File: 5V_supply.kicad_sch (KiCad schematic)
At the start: 25 parts

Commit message: little change
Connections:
- net VCC is gone; now on net 24V_supply: Q?.5 (D), Q?.6 (D), Q?.7 (D), Q?.8 (D)
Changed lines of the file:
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@@
   (junction (at 133.35 101.6) (diameter 0) (color 0 0 0 0)
   )
-  (junction (at 157.48 69.85) (diameter 0) (color 0 0 0 0)
-  )
   (junction (at 181.61 97.79) (diameter 0) (color 0 0 0 0)
   )
@@
     (stroke (width 0) (type default) (color 0 0 0 0))
   )
+  (wire (pts (xy 157.48 53.34) (xy 157.48 72.39))
+    (stroke (width 0) (type default) (color 0 0 0 0))
+  )
   (wire (pts (xy 102.87 95.25) (xy 102.87 97.79))
     (stroke (width 0) (type default) (color 0 0 0 0))
@@
     (stroke (width 0) (type default) (color 0 0 0 0))
   )
+  (wire (pts (xy 73.66 62.23) (xy 73.66 53.34))
+    (stroke (width 0) (type default) (color 0 0 0 0))
+  )
   (wire (pts (xy 118.11 69.85) (xy 118.11 74.93))
     (stroke (width 0) (type default) (color 0 0 0 0))
@@
     (stroke (width 0) (type default) (color 0 0 0 0))
   )
-  (wire (pts (xy 157.48 67.31) (xy 157.48 69.85))
-    (stroke (width 0) (type default) (color 0 0 0 0))
-  )
   (wire (pts (xy 110.49 62.23) (xy 110.49 69.85))
     (stroke (width 0) (type default) (color 0 0 0 0))
@@
     (stroke (width 0) (type default) (color 0 0 0 0))
   )
-  (wire (pts (xy 157.48 69.85) (xy 157.48 72.39))
-    (stroke (width 0) (type default) (color 0 0 0 0))
-  )
   (wire (pts (xy 130.81 92.71) (xy 149.86 92.71))
     (stroke (width 0) (type default) (color 0 0 0 0))
@@
   )
   (wire (pts (xy 186.69 82.55) (xy 194.31 82.55))
+    (stroke (width 0) (type default) (color 0 0 0 0))
+  )
+  (wire (pts (xy 73.66 53.34) (xy 157.48 53.34))
     (stroke (width 0) (type default) (color 0 0 0 0))
   )
@@
     (pin "2")
   )
-  (symbol (lib_id "power:VCC") (at 157.48 69.85 0) (unit 1)
-    (in_bom yes) (on_board yes) (fields_autoplaced)
-    (property "Reference" "#PWR?" (id 0) (at 157.48 73.66 0)
-      (effects (font (size 1.27 1.27)) hide)
-    )
-    (property "Value" "VCC" (id 1) (at 157.48 66.2455 0))
-    (property "Footprint" "" (id 2) (at 157.48 69.85 0)
-      (effects (font (size 1.27 1.27)) hide)
-    )
-    (property "Datasheet" "" (id 3) (at 157.48 69.85 0)
-      (effects (font (size 1.27 1.27)) hide)
-    )
-    (pin "1")
-  )
   (symbol (lib_id "Device:R") (at 139.7 101.6 90) (unit 1)

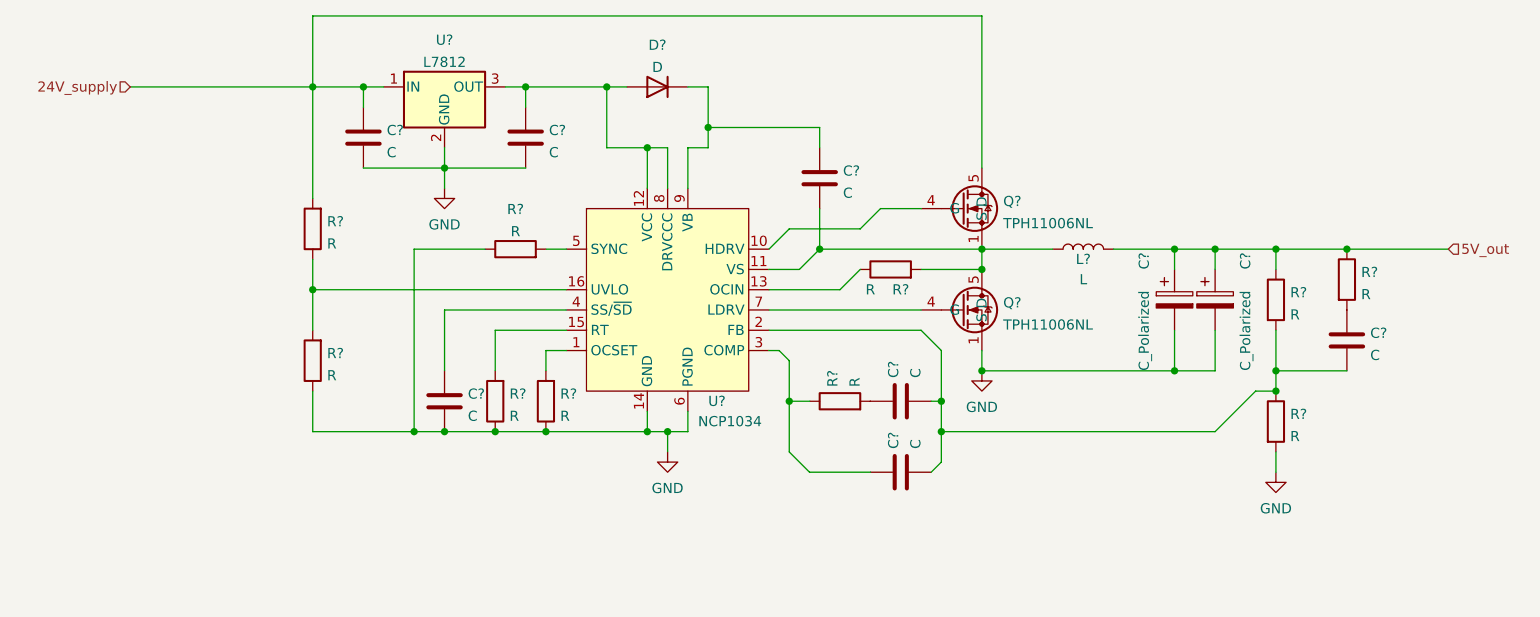
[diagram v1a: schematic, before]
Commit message: DC-DC pram setted
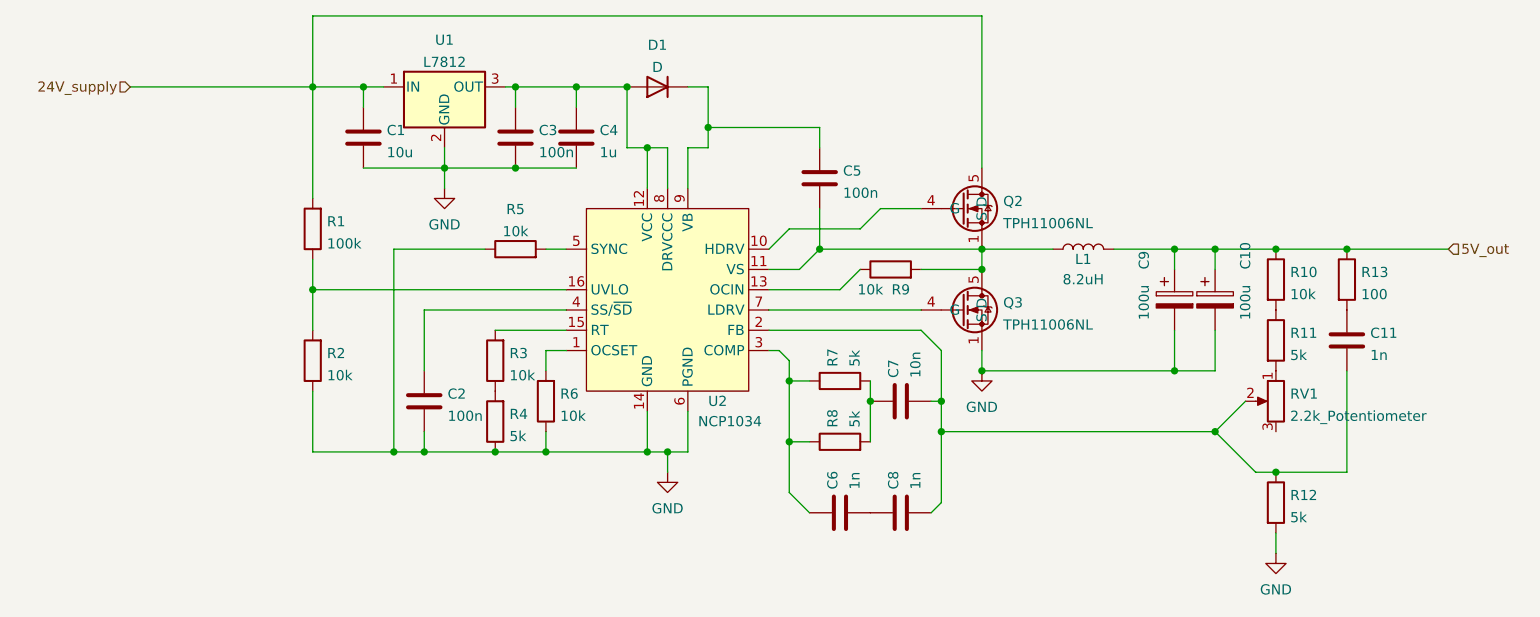
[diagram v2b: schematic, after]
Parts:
- added C3: 100n, symbol Device:C
- added C6: 1n, symbol Device:C
- added R11, R4, R7: 5k, symbol Device:R
- added RV1: 2.2k_Potentiometer, symbol Device:R_Potentiometer
- C1: renamed from C?; value C -> 10u
- C10, C9: renamed from C?; value C_Polarized -> 100u
- C11, C8: renamed from C?; value C -> 1n
- C2, C5: renamed from C?; value C -> 100n
- C4: renamed from C?; value C -> 1u
- C7: renamed from C?; value C -> 10n
- L1: renamed from L?; value L -> 8.2uH; footprint (none) -> Inductor_SMD:L_Vishay_IHLP-6767
- R1: renamed from R?; value R -> 100k
- R10, R2, R3, R5, R6, R9: renamed from R?; value R -> 10k
- R12, R8: renamed from R?; value R -> 5k
- R13: renamed from R?; value R -> 100
- gave numbers to parts that had none: 5
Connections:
- net GND: now also C3.2, R4.1; no longer R3.1
- net at C4.1, D1.2 (A), U1.3 (OUT)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: now also C3.1
- net at R8.1, U2.3 (COMP): now also C6.1, R7.1; no longer C8.1
- net at C11.2, C7.1, C8.2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: now also RV1.2; no longer R10.2
- net at C7.2, R8.2: now also R7.2
- new net: C6.2, C8.1
- new net: R10.2, R11.1
- new net: R11.2, RV1.1
- new net: R3.1, R4.2
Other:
- moved on the sheet: C2, C4, C8, R10, R12, R3, R8

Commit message: connectors
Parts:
- C1: footprint (none) -> Capacitor_SMD:C_0805_2012Metric
- C10, C9: footprint (none) -> Capacitor_SMD:CP_Elec_6.3x7.7
- C11, C2, C3, C4, C5, C6, C7, C8: footprint (none) -> Capacitor_SMD:C_0603_1608Metric
- D1: footprint (none) -> Diode_SMD:D_SOD-123
- R1, R10, R11, R12, R13, R2, R3, R4, R5, R6, R7, R8, R9: footprint (none) -> Resistor_SMD:R_0603_1608Metric
- U1: footprint (none) -> Package_TO_SOT_SMD:TO-252-2
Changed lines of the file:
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@@
       (effects (font (size 1.27 1.27)) (justify left))
     )
-    (property "Footprint" "" (id 2) (at 100.0252 72.39 0)
+    (property "Footprint" "Capacitor_SMD:C_0603_1608Metric" (id 2) (at 100.0252 72.39 0)
       (effects (font (size 1.27 1.27)) hide)
     )
@@
       (effects (font (size 1.27 1.27)) (justify left))
     )
-    (property "Footprint" "" (id 2) (at 187.6552 92.71 0)
+    (property "Footprint" "Capacitor_SMD:CP_Elec_6.3x7.7" (id 2) (at 187.6552 92.71 0)
       (effects (font (size 1.27 1.27)) hide)
     )
@@
       (effects (font (size 1.27 1.27)) (justify left))
     )
-    (property "Footprint" "" (id 2) (at 143.51 114.6048 0)
+    (property "Footprint" "Capacitor_SMD:C_0603_1608Metric" (id 2) (at 143.51 114.6048 0)
       (effects (font (size 1.27 1.27)) hide)
     )
@@
       (effects (font (size 1.27 1.27)) (justify left))
     )
-    (property "Footprint" "" (id 2) (at 138.1252 77.47 0)
+    (property "Footprint" "Capacitor_SMD:C_0603_1608Metric" (id 2) (at 138.1252 77.47 0)
       (effects (font (size 1.27 1.27)) hide)
     )
@@
     (property "Reference" "R5" (id 0) (at 99.06 77.5675 90))
     (property "Value" "10k" (id 1) (at 99.06 80.3426 90))
-    (property "Footprint" "" (id 2) (at 99.06 84.328 90)
+    (property "Footprint" "Resistor_SMD:R_0603_1608Metric" (id 2) (at 99.06 84.328 90)
       (effects (font (size 1.27 1.27)) hide)
     )
@@
     (property "Reference" "U1" (id 0) (at 90.17 56.3585 0))
     (property "Value" "L7812" (id 1) (at 90.17 59.1336 0))
-    (property "Footprint" "" (id 2) (at 90.805 66.04 0)
+    (property "Footprint" "Package_TO_SOT_SMD:TO-252-2" (id 2) (at 90.805 66.04 0)
       (effects (font (size 1.27 1.27) italic) (justify left) hide)
     )
@@
     (property "Reference" "D1" (id 0) (at 116.84 56.9935 0))
     (property "Value" "D" (id 1) (at 116.84 59.7686 0))
-    (property "Footprint" "" (id 2) (at 116.84 62.23 0)
+    (property "Footprint" "Diode_SMD:D_SOD-123" (id 2) (at 116.84 62.23 0)
       (effects (font (size 1.27 1.27)) hide)
     )
@@
       (effects (font (size 1.27 1.27)) (justify right))
     )
-    (property "Footprint" "" (id 2) (at 104.648 101.6 90)
+    (property "Footprint" "Resistor_SMD:R_0603_1608Metric" (id 2) (at 104.648 101.6 90)
       (effects (font (size 1.27 1.27)) hide)
     )
@@
       (effects (font (size 1.27 1.27)) (justify left))
     )
-    (property "Footprint" "" (id 2) (at 151.13 114.6048 0)
+    (property "Footprint" "Capacitor_SMD:C_0603_1608Metric" (id 2) (at 151.13 114.6048 0)
       (effects (font (size 1.27 1.27)) hide)
     )
@@
       (effects (font (size 1.27 1.27)) (justify right))
     )
-    (property "Footprint" "" (id 2) (at 143.51 102.5652 0)
+    (property "Footprint" "Capacitor_SMD:C_0603_1608Metric" (id 2) (at 143.51 102.5652 0)
       (effects (font (size 1.27 1.27)) hide)
     )
@@
       (effects (font (size 1.27 1.27)) (justify left))
     )
-    (property "Footprint" "" (id 2) (at 192.532 86.36 90)
+    (property "Footprint" "Resistor_SMD:R_0603_1608Metric" (id 2) (at 192.532 86.36 90)
       (effects (font (size 1.27 1.27)) hide)
     )
@@
       (effects (font (size 1.27 1.27)) (justify right))
     )
-    (property "Footprint" "" (id 2) (at 75.438 80.01 90)
+    (property "Footprint" "Resistor_SMD:R_0603_1608Metric" (id 2) (at 75.438 80.01 90)
       (effects (font (size 1.27 1.27)) hide)
     )
@@
       (effects (font (size 1.27 1.27)) (justify left))
     )
-    (property "Footprint" "" (id 2) (at 80.9752 72.39 0)
+    (property "Footprint" "Capacitor_SMD:C_0805_2012Metric" (id 2) (at 80.9752 72.39 0)
       (effects (font (size 1.27 1.27)) hide)
     )
@@
       (effects (font (size 1.27 1.27)) (justify left))
     )
-    (property "Footprint" "" (id 2) (at 201.422 86.36 90)
+    (property "Footprint" "Resistor_SMD:R_0603_1608Metric" (id 2) (at 201.422 86.36 90)
       (effects (font (size 1.27 1.27)) hide)
     )
@@
       (effects (font (size 1.27 1.27)) (justify left))
     )
-    (property "Footprint" "" (id 2) (at 192.532 114.3 90)
+    (property "Footprint" "Resistor_SMD:R_0603_1608Metric" (id 2) (at 192.532 114.3 90)
       (effects (font (size 1.27 1.27)) hide)
     )
@@
     (property "Reference" "R9" (id 0) (at 147.32 87.63 90))
     (property "Value" "10k" (id 1) (at 143.51 87.63 90))
-    (property "Footprint" "" (id 2) (at 146.05 86.868 90)
+    (property "Footprint" "Resistor_SMD:R_0603_1608Metric" (id 2) (at 146.05 86.868 90)
       (effects (font (size 1.27 1.27)) hide)
     )
@@
       (effects (font (size 1.27 1.27)) (justify left))
     )
-    (property "Footprint" "" (id 2) (at 88.5952 105.41 0)
+    (property "Footprint" "Capacitor_SMD:C_0603_1608Metric" (id 2) (at 88.5952 105.41 0)
       (effects (font (size 1.27 1.27)) hide)
     )
@@
       (effects (font (size 1.27 1.27)) (justify left))
     )
-    (property "Footprint" "" (id 2) (at 182.5752 92.71 0)
+    (property "Footprint" "Capacitor_SMD:CP_Elec_6.3x7.7" (id 2) (at 182.5752 92.71 0)
       (effects (font (size 1.27 1.27)) hide)
     )
@@
       (effects (font (size 1.27 1.27)) (justify left))
     )
-    (property "Footprint" "" (id 2) (at 192.532 93.98 90)
+    (property "Footprint" "Resistor_SMD:R_0603_1608Metric" (id 2) (at 192.532 93.98 90)
       (effects (font (size 1.27 1.27)) hide)
     )
@@
       (effects (font (size 1.27 1.27)) (justify left))
     )
-    (property "Footprint" "" (id 2) (at 107.6452 72.39 0)
+    (property "Footprint" "Capacitor_SMD:C_0603_1608Metric" (id 2) (at 107.6452 72.39 0)
       (effects (font (size 1.27 1.27)) hide)
     )
@@
       (effects (font (size 1.27 1.27)) (justify right))
     )
-    (property "Footprint" "" (id 2) (at 75.438 96.52 90)
+    (property "Footprint" "Resistor_SMD:R_0603_1608Metric" (id 2) (at 75.438 96.52 90)
       (effects (font (size 1.27 1.27)) hide)
     )
@@
       (effects (font (size 1.27 1.27)) (justify right))
     )
-    (property "Footprint" "" (id 2) (at 98.298 96.52 90)
+    (property "Footprint" "Resistor_SMD:R_0603_1608Metric" (id 2) (at 98.298 96.52 90)
       (effects (font (size 1.27 1.27)) hide)
     )
@@
       (effects (font (size 1.27 1.27)) (justify right))
     )
-    (property "Footprint" "" (id 2) (at 98.298 104.14 90)
+    (property "Footprint" "Resistor_SMD:R_0603_1608Metric" (id 2) (at 98.298 104.14 90)
       (effects (font (size 1.27 1.27)) hide)
     )
@@
       (effects (font (size 1.27 1.27)) (justify left))
     )
-    (property "Footprint" "" (id 2) (at 139.7 108.458 90)
+    (property "Footprint" "Resistor_SMD:R_0603_1608Metric" (id 2) (at 139.7 108.458 90)
       (effects (font (size 1.27 1.27)) hide)
     )
@@
       (effects (font (size 1.27 1.27)) (justify left))
     )
-    (property "Footprint" "" (id 2) (at 139.7 100.838 90)
+    (property "Footprint" "Resistor_SMD:R_0603_1608Metric" (id 2) (at 139.7 100.838 90)
       (effects (font (size 1.27 1.27)) hide)
     )
@@
       (effects (font (size 1.27 1.27)) (justify left))
     )
-    (property "Footprint" "" (id 2) (at 204.1652 97.79 0)
-      (effects (font (size 1.27 1.27)) hide)
-    )
+    (property "Footprint" "Capacitor_SMD:C_0603_1608Metric" (id 2) (at 204.1652 97.79 0)
+      (effects (font (size 1.27 1.27)) hide)
+    )

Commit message: many
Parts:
- RV1: footprint (none) -> Potentiometer_additional:Potentiometer_Murata_PVZ3A
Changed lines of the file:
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@@
       (effects (font (size 1.27 1.27)) (justify right))
     )
-    (property "Footprint" "" (id 2) (at 194.31 101.6 0)
+    (property "Footprint" "Potentiometer_additional:Potentiometer_Murata_PVZ3A" (id 2) (at 194.31 101.6 0)
       (effects (font (size 1.27 1.27)) hide)
     )
